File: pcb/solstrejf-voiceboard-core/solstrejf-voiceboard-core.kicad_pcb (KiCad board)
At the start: 2 copper layers, 121.9 x 90.2 mm, 123 parts, among them J1 PSU+Power Connector, J2 Mod-Matrix Connector, J3 Direct_Out, J4 Front Panel Connector, U1 AS3372E, U2 L78L05, U3 L79L05, U4 TL072, U5 LM324, U6 ONESHOT, U7 L78L12, U8 L79L12

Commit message: Layout work-in-progress..
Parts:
- moved TP1 153.8 mm to (110.5, 130.8)
- moved TP2 149.2 mm to (115.6, 130.8)
- moved TP3 145.1 mm to (120.7, 130.8)
- moved J1 142.0 mm to (90.2, 133.3), turned to 90 degrees
- moved U2 122.1 mm to (134.6, 111.8)
- moved U3 120.7 mm to (141.0, 111.8)
- moved C9 117.4 mm to (139.7, 120.7)
- moved R6 113.7 mm to (151.1, 132.1), turned to 180 degrees
- moved R5 113.1 mm to (151.1, 128.3), turned to 180 degrees
- moved C10 112.2 mm to (147.3, 120.7)
- moved D1 104.2 mm to (154.9, 128.3)
- moved C5 103.9 mm to (125.7, 128.3)
- moved C8 103.2 mm to (133.3, 132.1)
- moved C7 103.0 mm to (133.3, 128.3)
- moved C6 102.5 mm to (125.7, 132.1)
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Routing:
- net /FREQUENCY_CV/virtual_gnd_freqcv: track 0.00 -> 51.3 mm
- net Net-(U2-VI): track 0.00 -> 44.7 mm
- net /PAN_CV/virtual_gnd_pancv: track 0.00 -> 44.4 mm
- net /FREQUENCY_CV/CLIP_-_FREQ: track 0.00 -> 43.5 mm
- net /FREQUENCY_CV/CLIP_+_FREQ: track 0.00 -> 41.1 mm
- net /PAN_CV: track 0.00 -> 36.3 mm
- net +15V: track 2.54 -> 36.0 mm
- net -15V: track 2.54 -> 31.8 mm
- net Net-(U3-VI): track 0.00 -> 26.7 mm
- net +12V: track 0.00 -> 22.2 mm
- net -12V: track 0.00 -> 22.0 mm
- net -5V: track 2.54 -> 21.6 mm
- net +5V: track 4.36 -> 22.2 mm
- net /PAN_CV/CLIP_+_PAN: track 0.00 -> 14.6 mm
- net /FREQUENCY_CV/FREQ_CV_prescale: track 0.00 -> 12.7 mm
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- added copper zone on F.Cu, net /FREQUENCY_CV/virtual_gnd_freqcv
- added copper zone on F.Cu, net /PAN_CV/virtual_gnd_pancv

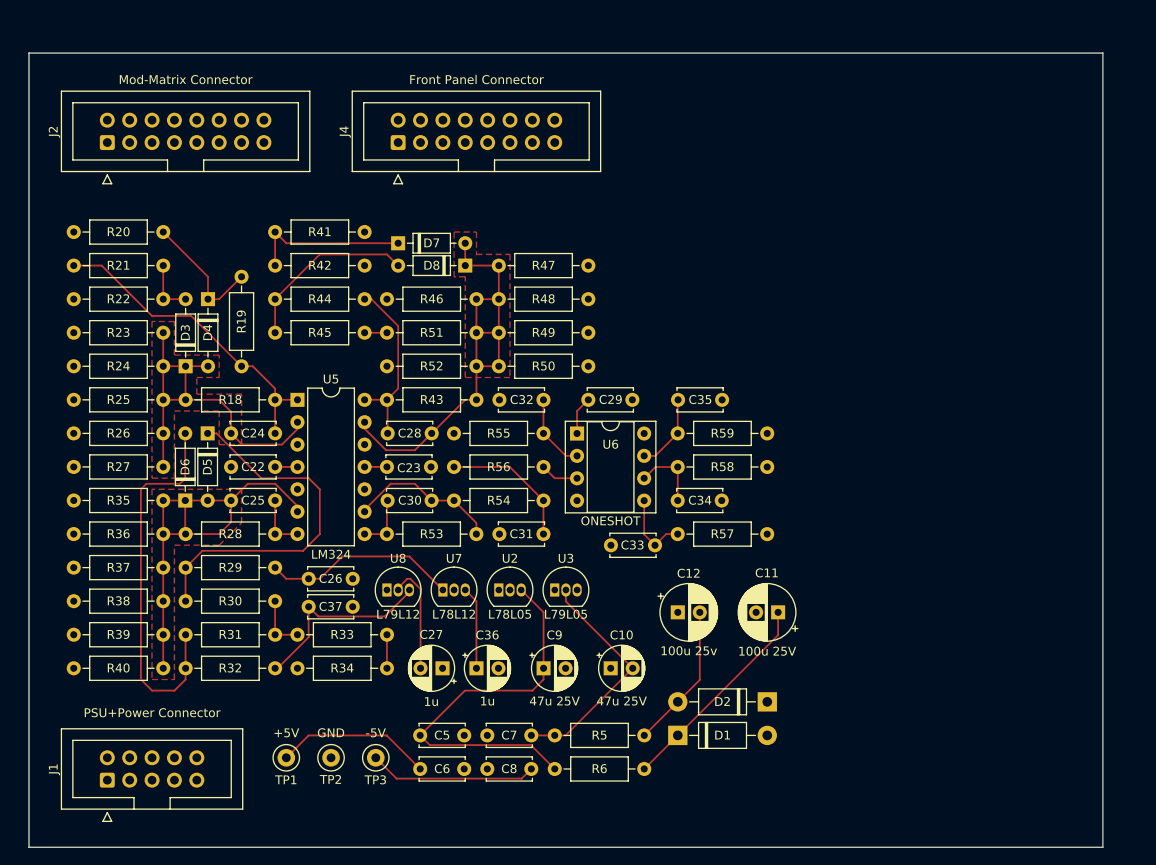
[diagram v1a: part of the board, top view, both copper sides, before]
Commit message: Added M3 mounting holes to schematic/PCB and worked on power/regulator layout
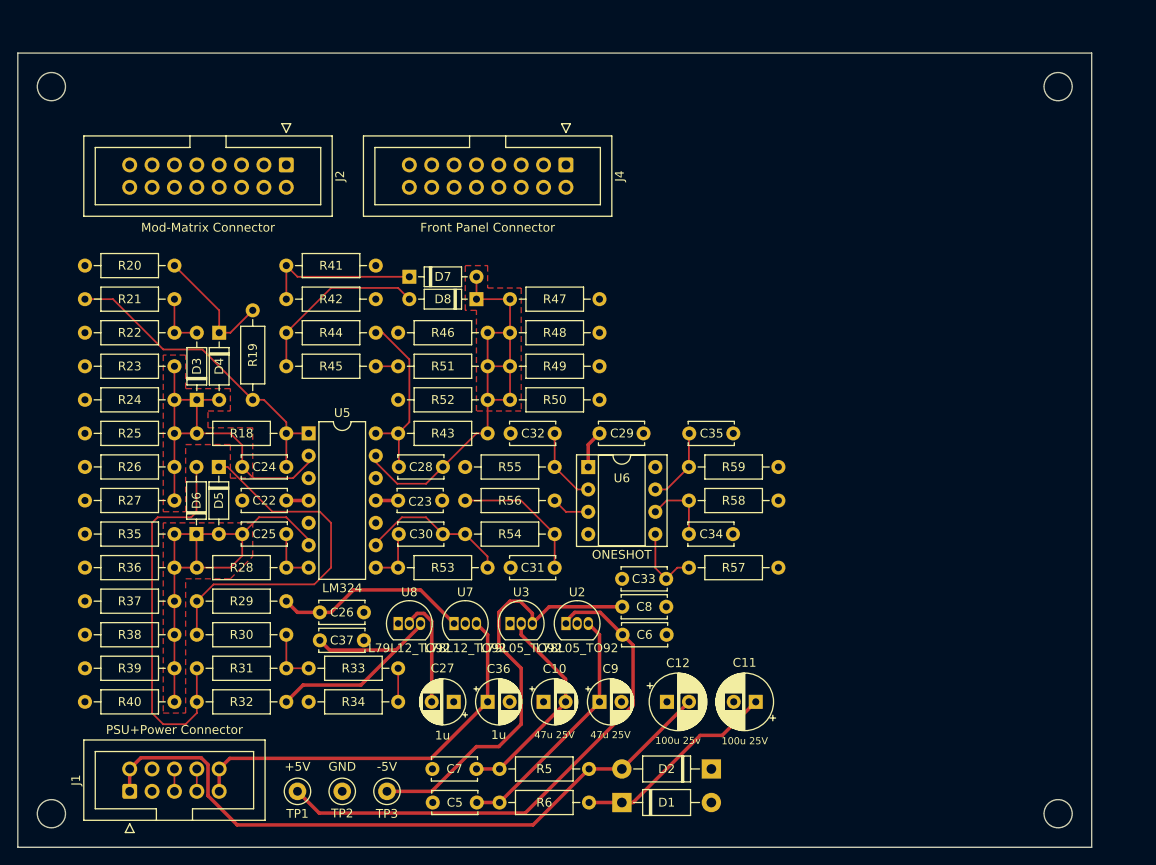
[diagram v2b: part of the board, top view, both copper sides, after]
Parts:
- added H1: M3, MountingHole:MountingHole_3.2mm_M3_DIN965, F.Cu at (83.8, 54.6)
- added H2: M3, MountingHole:MountingHole_3.2mm_M3_DIN965, F.Cu at (83.8, 137.2)
- added H3: M3, MountingHole:MountingHole_3.2mm_M3_DIN965, F.Cu at (198.1, 54.6)
- added H4: M3, MountingHole:MountingHole_3.2mm_M3_DIN965, F.Cu at (198.1, 137.2)
- U2: value L78L05 -> L78L05_TO92
- U3: value L79L05 -> L79L05_TO92
- U7: value L78L12 -> L78L12_TO92
- U8: value L79L12 -> L79L12_TO92
- moved C6 27.6 mm to (148.7, 116.8)
- moved C8 27.4 mm to (153.6, 113.7), turned to 180 degrees
- moved J2 20.5 mm to (110.5, 63.5), turned to -90 degrees
- moved J4 19.2 mm to (142.2, 63.5), turned to -90 degrees
- moved C11 10.5 mm to (163.8, 124.5)
- moved C12 10.2 mm to (153.7, 124.5)
- moved C5 9.97 mm to (132.1, 135.9), turned to 180 degrees
- moved D2 9.92 mm to (158.8, 132.1)
- moved D1 9.92 mm to (148.6, 135.9)
- moved C10 8.52 mm to (139.7, 124.5)
- moved U2 8.52 mm to (142.2, 115.6)
- moved C9 7.41 mm to (146.1, 124.5)
- moved R5 7.34 mm to (144.9, 132.1)
- moved R6 7.34 mm to (144.9, 135.9)
- moved C7 7.30 mm to (127.1, 132.1)
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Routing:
- net -15V: track 31.8 -> 93.0 mm
- net +5V: track 22.2 -> 65.2 mm
- net +15V: track 36.0 -> 71.8 mm
- net -5V: track 21.6 -> 51.7 mm
- net Net-(U2-VI): track 44.7 -> 28.1 mm
- net -12V: track 22.0 -> 28.4 mm
- net /R_OUT: track 0.00 -> 2.54 mm
- net /L_OUT: track 0.00 -> 2.54 mm
- net Net-(U3-VI): track 26.7 -> 24.3 mm

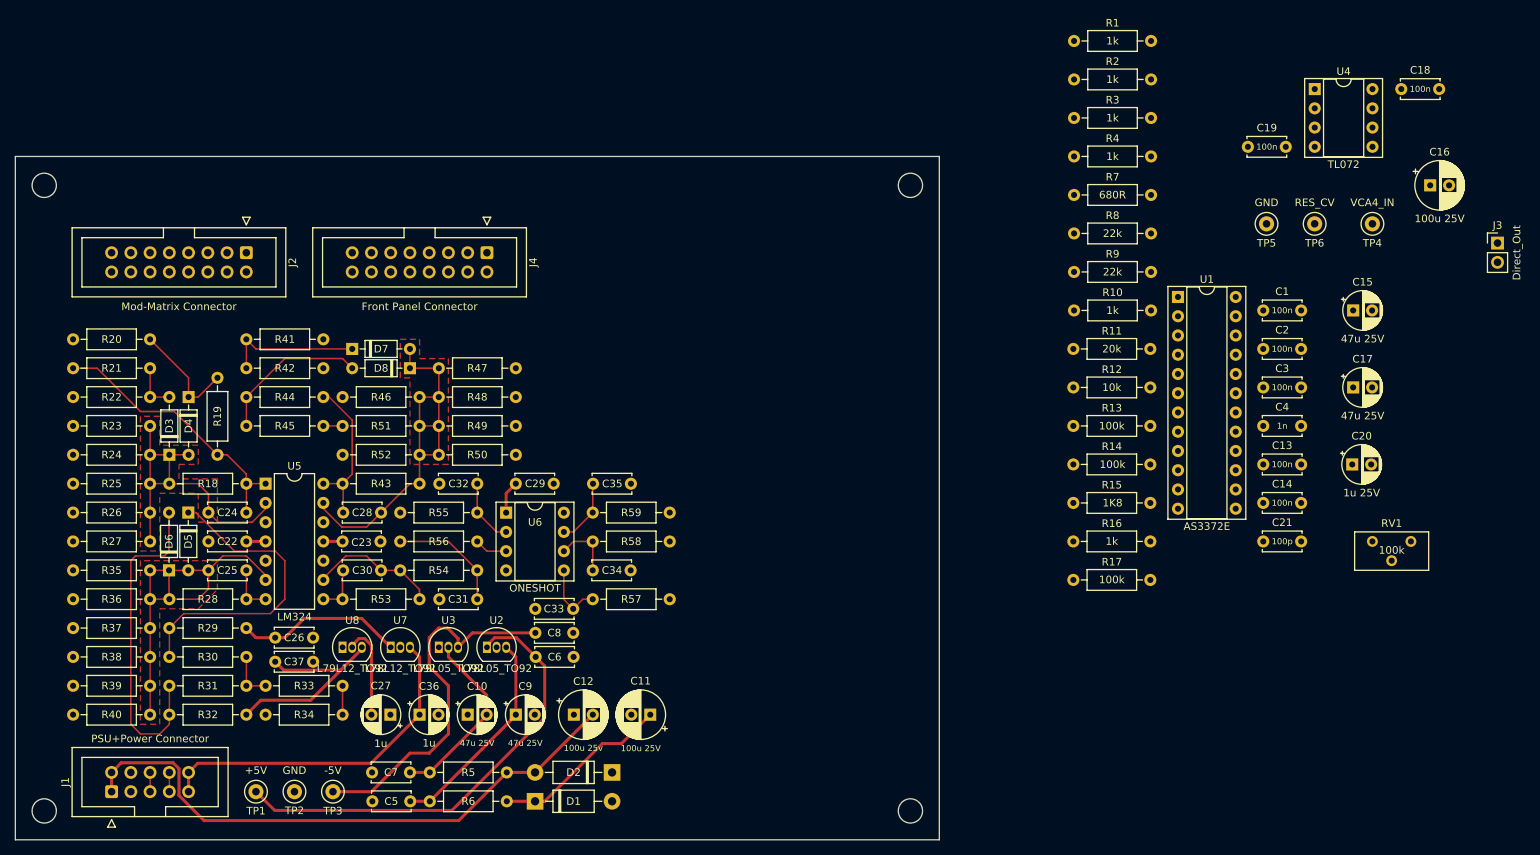
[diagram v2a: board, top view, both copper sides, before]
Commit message: Finish layout of the voice board. Included 3D renders in README.
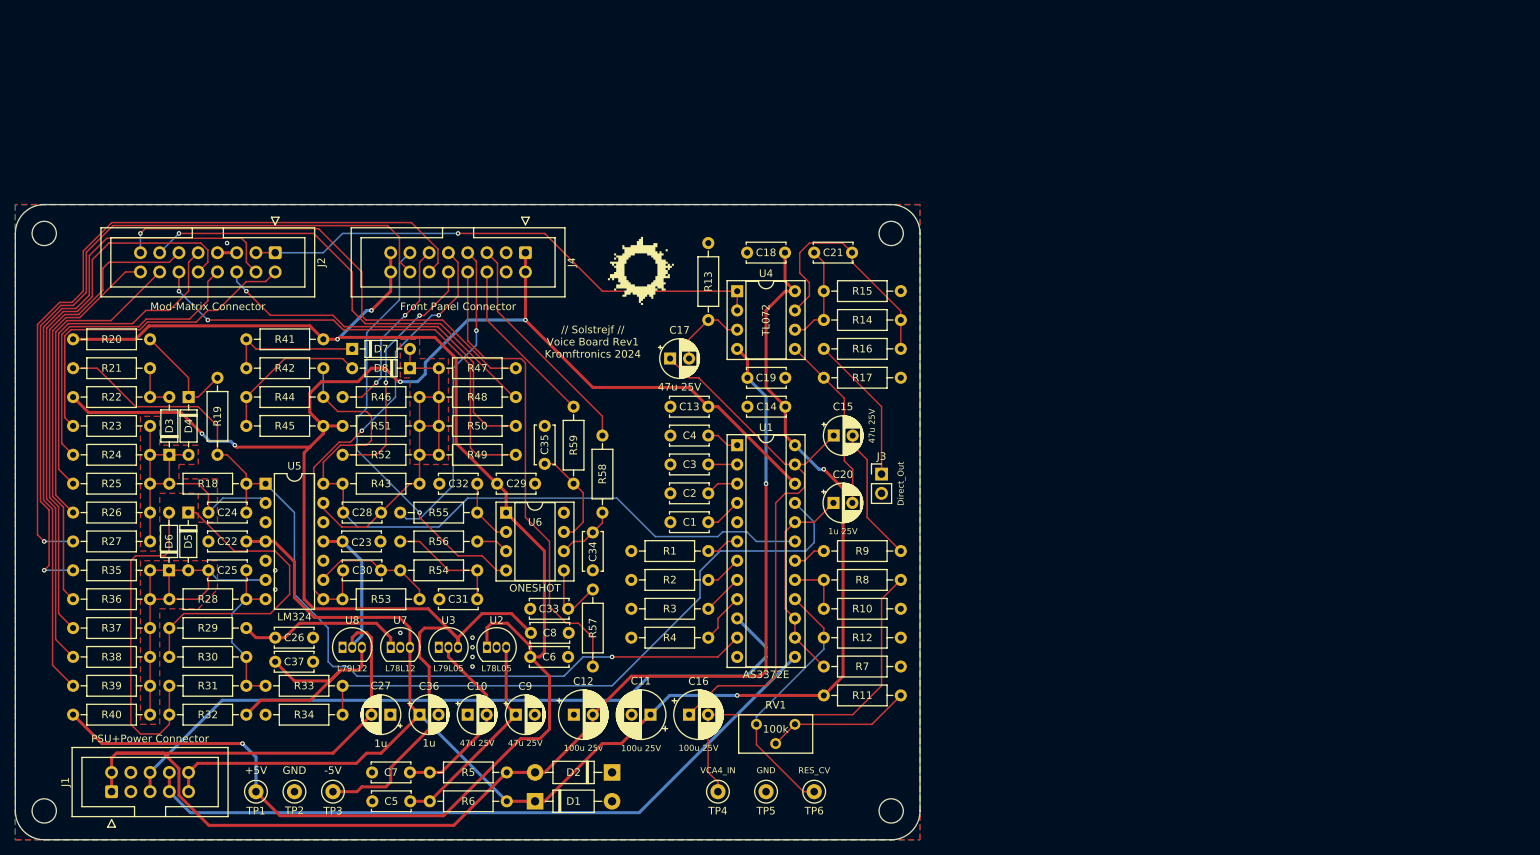
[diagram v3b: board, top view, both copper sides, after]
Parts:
- added G***: LOGO, LOGO, F.Cu at (162.6, 66.0)
- U2: value L78L05_TO92 -> L78L05
- U3: value L79L05_TO92 -> L79L05
- U7: value L78L12_TO92 -> L78L12
- U8: value L79L12_TO92 -> L79L12
- moved C16 120.2 mm to (168.9, 124.5)
- moved TP4 114.3 mm to (172.7, 134.6)
- moved TP5 99.9 mm to (179.1, 134.6)
- moved TP6 99.9 mm to (185.4, 134.6)
- moved C17 90.2 mm to (166.4, 77.5)
- moved R1 89.1 mm to (161.3, 102.9)
- moved R2 88.2 mm to (161.3, 106.7)
- moved R3 87.2 mm to (161.3, 110.5)
- moved J3 86.8 mm to (194.3, 92.7)
- moved R4 86.3 mm to (161.3, 114.3)
- moved RV1 84.8 mm to (182.9, 125.7)
- moved C18 84.1 mm to (181.6, 63.5), turned to 180 degrees
- moved U4 80.7 mm to (175.3, 68.6)
- moved C1 78.4 mm to (171.4, 99.1), turned to 180 degrees
- moved C2 75.7 mm to (171.4, 95.2), turned to 180 degrees
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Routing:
- net -5V: track 51.7 -> 226.9 mm, vias 0 -> 4
- net +5V: track 65.2 -> 211.4 mm, vias 0 -> 3
- net +15V: track 71.8 -> 208.0 mm, vias 0 -> 2
- net -15V: track 93.0 -> 218.9 mm, vias 0 -> 1
- net /PAN_POT: track 0.00 -> 99.3 mm, vias 0 -> 1
- net /FREQ_POT: track 0.00 -> 98.5 mm, vias 0 -> 1
- net /L_OUT: track 2.54 -> 96.8 mm
- net /R_OUT: track 2.54 -> 94.7 mm
- net /FREQ4: track 0.00 -> 88.2 mm
- net /PAN_CV: track 36.3 -> 122.3 mm, vias 0 -> 1
- net /FREQ_CV: track 3.81 -> 82.2 mm
- net /FREQ3: track 0.00 -> 77.4 mm
- net /AMP_CV: track 20.4 -> 96.0 mm
- net /VCF_OUT: track 0.00 -> 73.5 mm
- net /VOICE_TO_MOD: track 0.00 -> 70.2 mm, vias 0 -> 1
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- added copper zone on B.Cu, net GND
- added copper zone on F.Cu, net GND
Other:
- board size 121.9 x 90.2 mm -> 119.4 x 83.8 mm
- board text added: "// Solstrejf // Voice Board Rev1 Kromftronics 2024"
